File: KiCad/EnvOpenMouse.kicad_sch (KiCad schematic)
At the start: 69 parts, among them J10 FH12 12S 0.5SH, J2 Button, J3 Conn_01x05, J4 Conn_01x09, J5 Conn_02x02_Top_Bottom, J5 SKRKAEE020, J6 Conn_02x02_Top_Bottom, J7 Conn_02x02_Top_Bottom, J8 Conn_02x02_Top_Bottom, J9 Conn_01x03, SW1 SW_Push_SPDT, SW2 SW_Push_SPDT, SW3 SW_Push_SPDT, U1 AP2112K-3.3, U2 TLV70218DBVR, U3 BQ24074RGT, U3 RP2040, U4 PMW3360DM-T2QU, Y1 3225_4P 12MHz

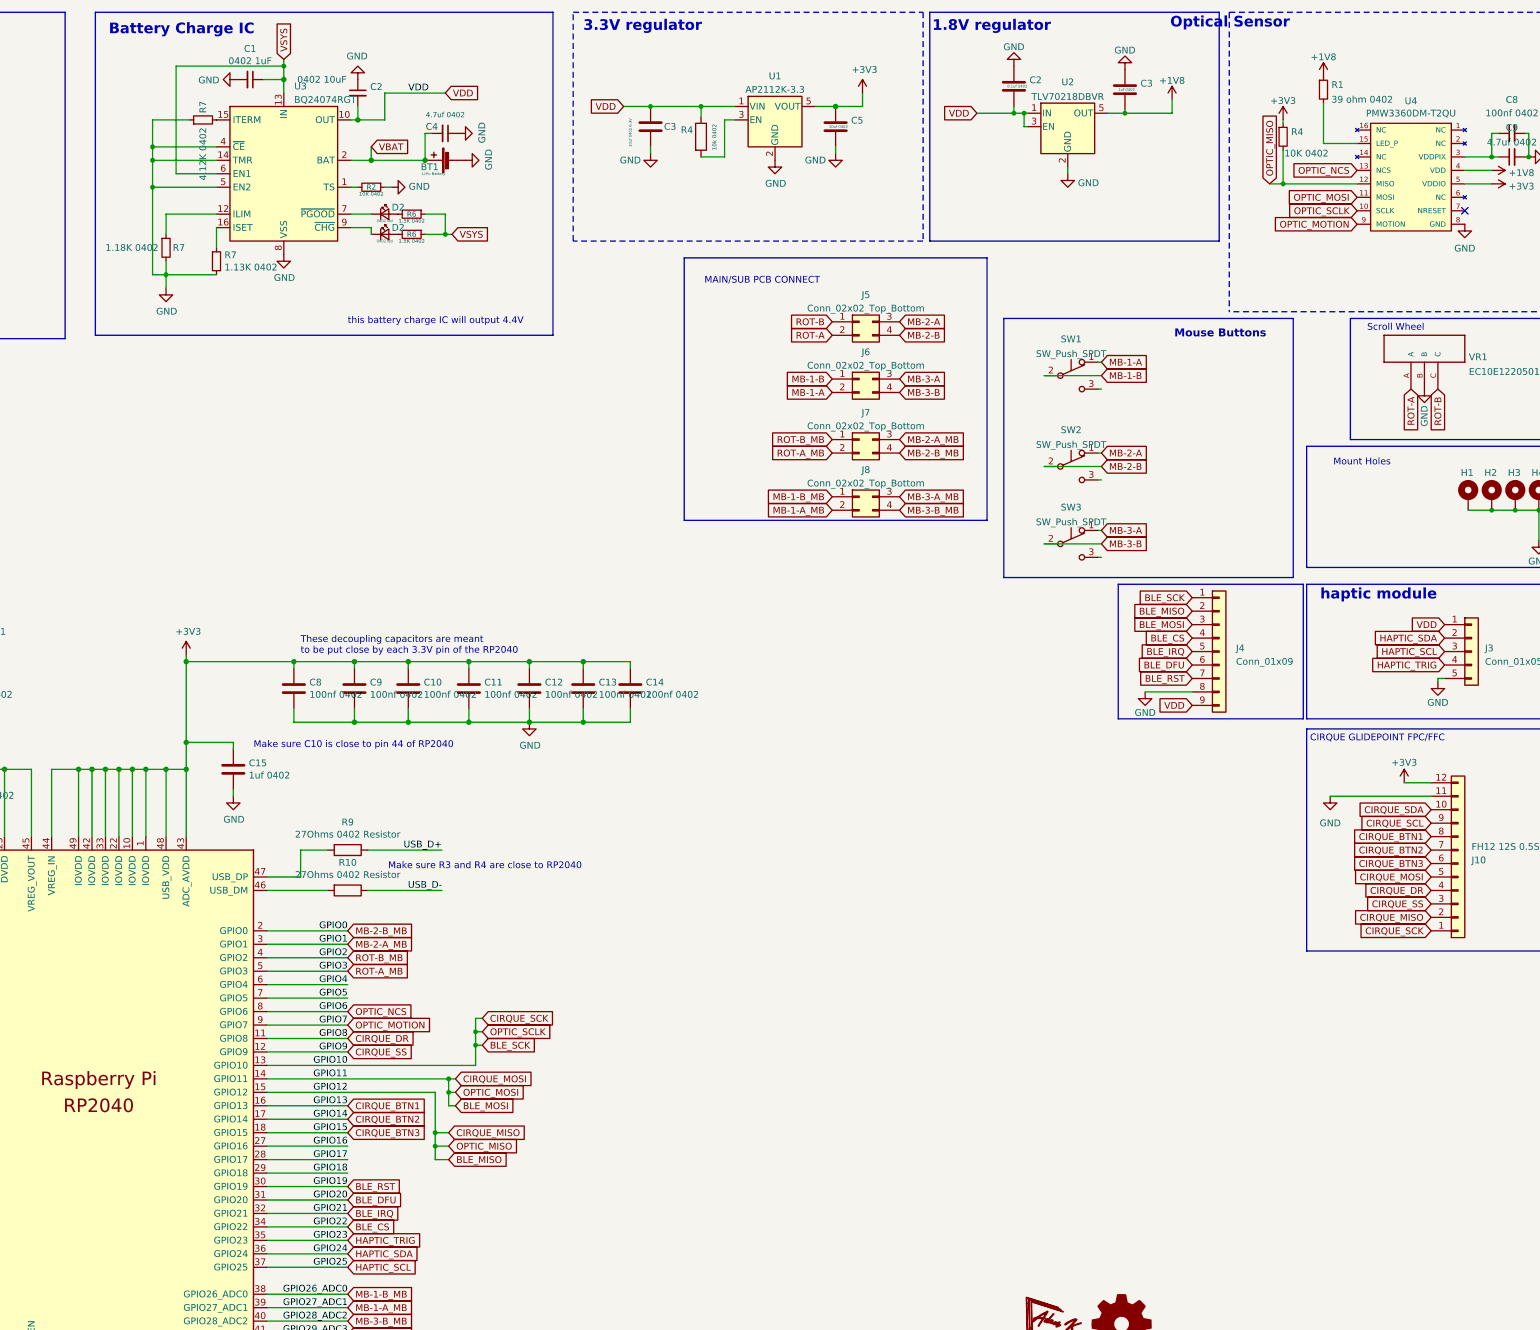
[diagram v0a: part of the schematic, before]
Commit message: re-worked PCB to remove wireless support and battery charge IC
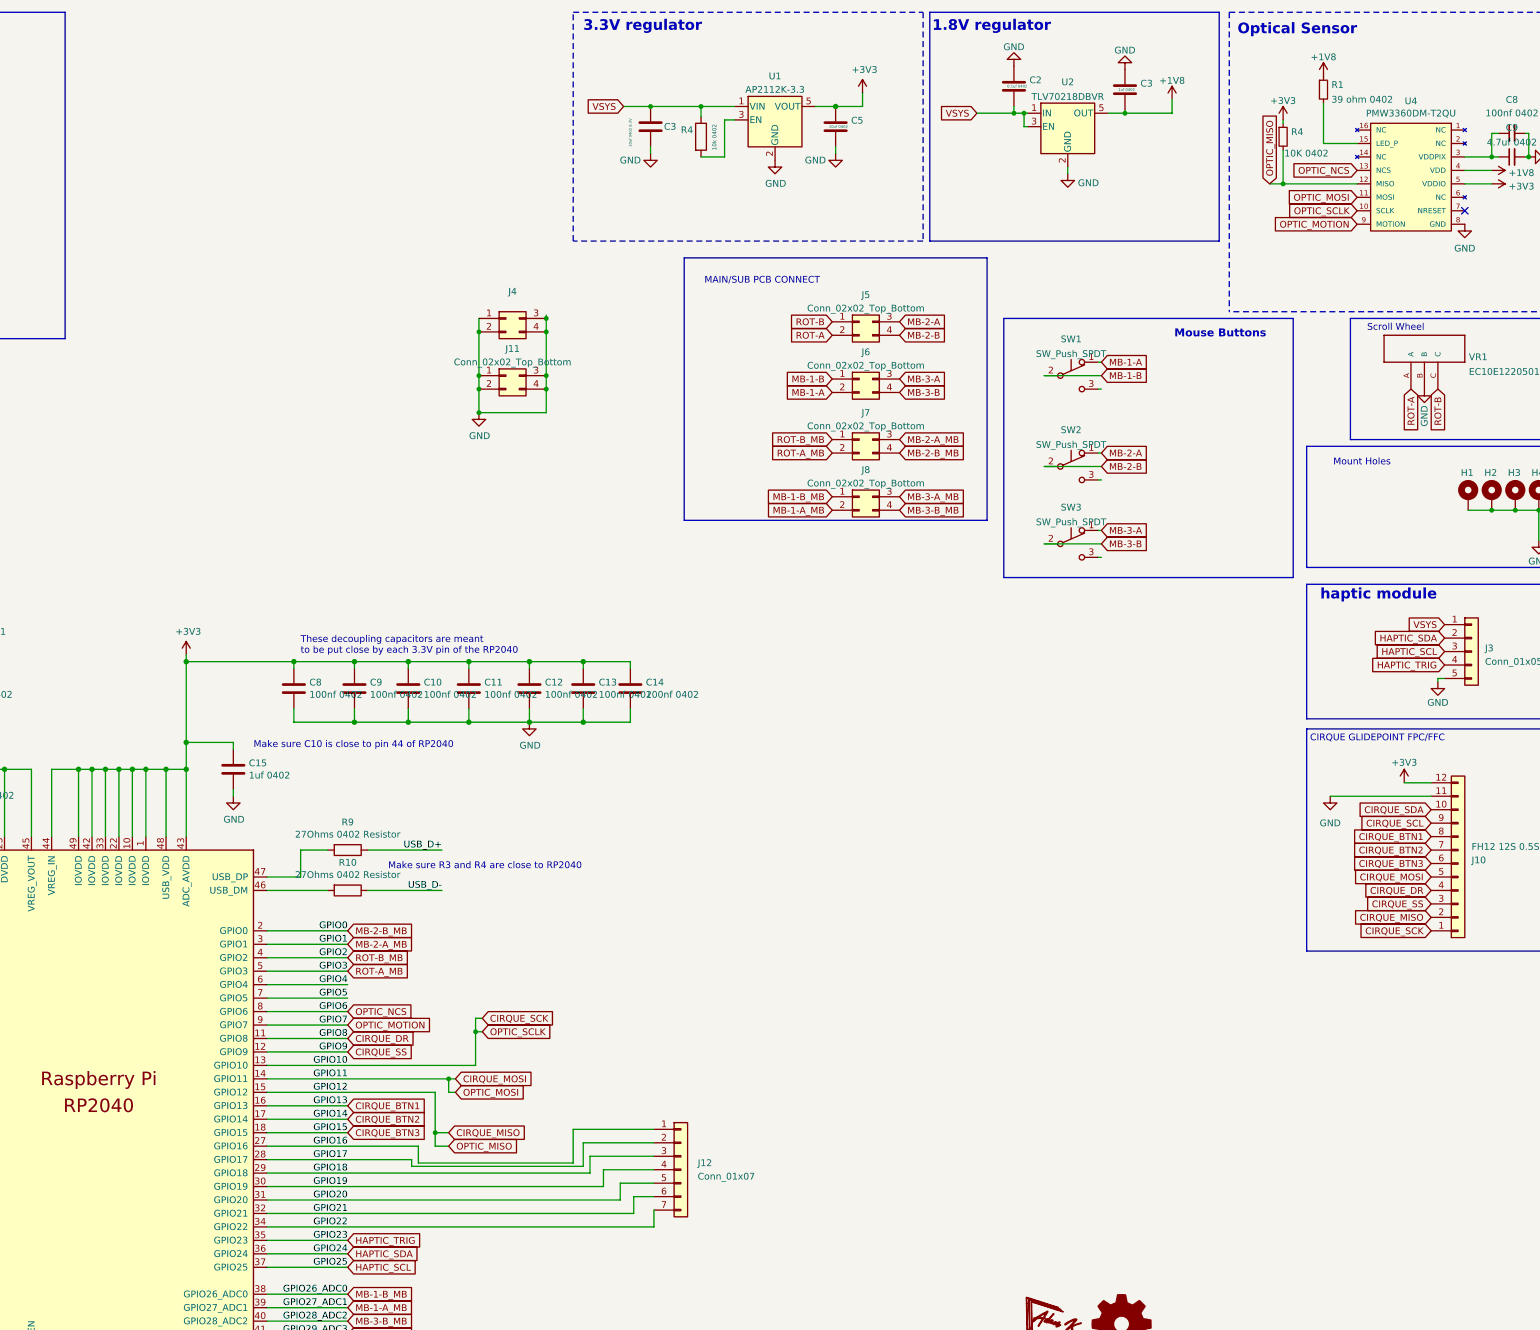
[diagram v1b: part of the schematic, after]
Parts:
- removed BT1: Li-Po Battery, Connector_JST:JST_PH_B2B-PH-K_1x02_P2.00mm_Vertical, symbol Device:Battery_Cell
- removed C1: 0402 1uF, Capacitor_SMD:C_0402_1005Metric, symbol Device:C_Small
- removed C2: 0402 10uF, Resistor_SMD:R_0402_1005Metric, symbol Device:C_Small
- removed C4: 4.7uf 0402, Capacitor_SMD:C_0402_1005Metric, symbol Device:C_Small
- removed D2 (x2): 0402 led, LED_SMD:LED_0402_1005Metric, symbol Device:LED_Small
- removed J4: Conn_01x09, Connector_PinHeader_2.54mm:PinHeader_1x09_P2.54mm_Vertical, symbol Connector_Generic:Conn_01x09
- removed R2: 10K 0402, Resistor_SMD:R_0402_1005Metric, symbol Device:R_Small
- removed R6 (x2): 1.5K 0402, Resistor_SMD:R_0402_1005Metric, symbol Device:R_Small
- removed R7: 1.13K 0402, Resistor_SMD:R_0402_1005Metric, symbol Device:R_Small
- removed R7: 1.18K 0402, Resistor_SMD:R_0402_1005Metric, symbol Device:R_Small
- removed R7: 4.12K 0402, Resistor_SMD:R_0402_1005Metric, symbol Device:R_Small
- removed U3: BQ24074RGT, Package_DFN_QFN:VQFN-16-1EP_3x3mm_P0.5mm_EP1.6x1.6mm, symbol Battery_Management:BQ24074RGT
- added J11, J4: Conn_02x02_Top_Bottom, Connector_PinHeader_1.27mm:PinHeader_1x02_P1.27mm_Vertical, symbol Connector_Generic:Conn_02x02_Top_Bottom
- added J12: Conn_01x07, Connector_PinHeader_1.00mm:PinHeader_1x07_P1.00mm_Vertical, symbol Connector_Generic:Conn_01x07
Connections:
- net VDD is gone; now on net VSYS: C2.2, C3.1, J3.1 (Pin_1), R4.1, U1.1 (VIN), U2.1 (IN), U2.3 (EN)
- net GND: now also J11.1 (Pin_1), J11.2 (Pin_2), J11.3 (Pin_3), J11.4 (Pin_4), J4.1 (Pin_1), J4.2 (Pin_2), J4.3 (Pin_3), J4.4 (Pin_4)
- net GPIO16: now also J12.1 (Pin_1)
- net GPIO17: now also J12.2 (Pin_2)
- net GPIO18: now also J12.3 (Pin_3)
- net BLE_CS renamed GPIO22
- net GPIO22: now also J12.7 (Pin_7)
- net BLE_DFU renamed GPIO20
- net GPIO20: now also J12.5 (Pin_5)
- net BLE_IRQ renamed GPIO21
- net GPIO21: now also J12.6 (Pin_6)
- net BLE_MISO renamed CIRQUE_MISO
- net BLE_MOSI renamed CIRQUE_MOSI
- net BLE_RST renamed GPIO19
- net GPIO19: now also J12.4 (Pin_4)
- net BLE_SCK renamed CIRQUE_SCK
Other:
- note removed: "Battery Charge IC"
- note removed: "this battery charge IC will output 4.4V"

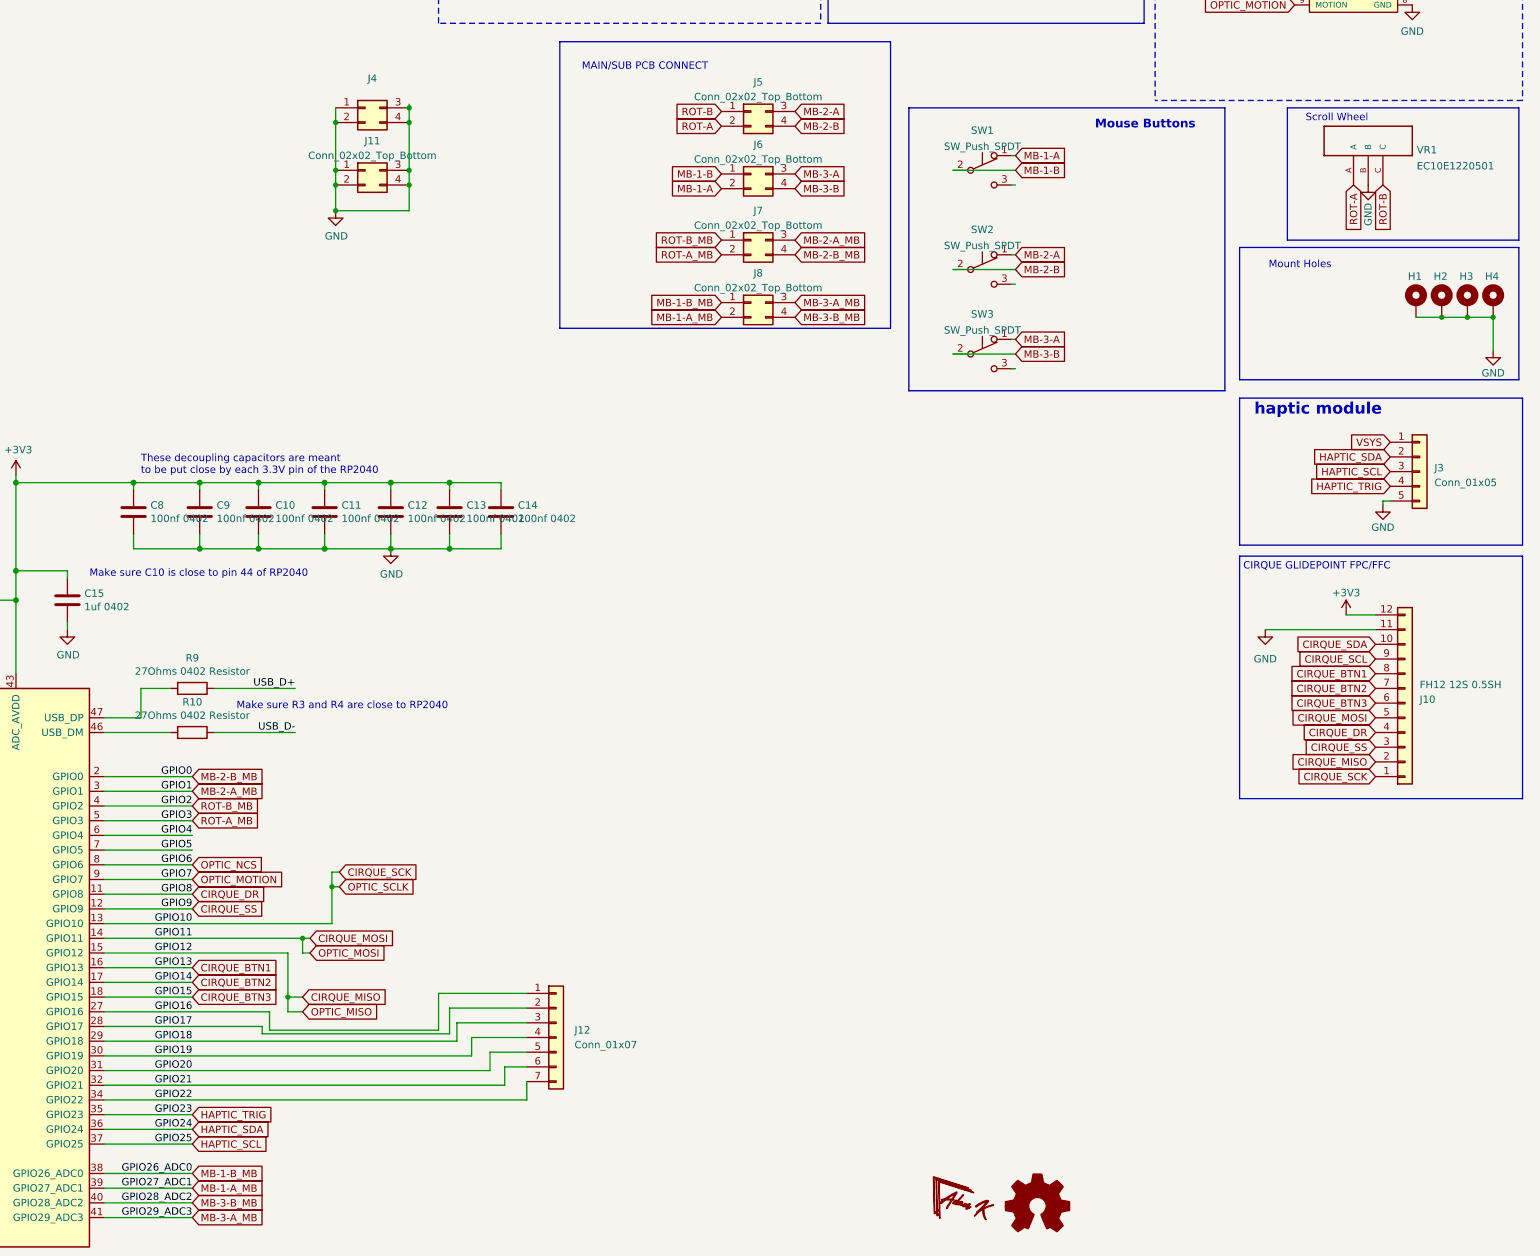
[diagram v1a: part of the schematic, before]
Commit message: removed a bunch of headers, added proper zones for 3v3 and 1v1, would like to add 4x side buttons
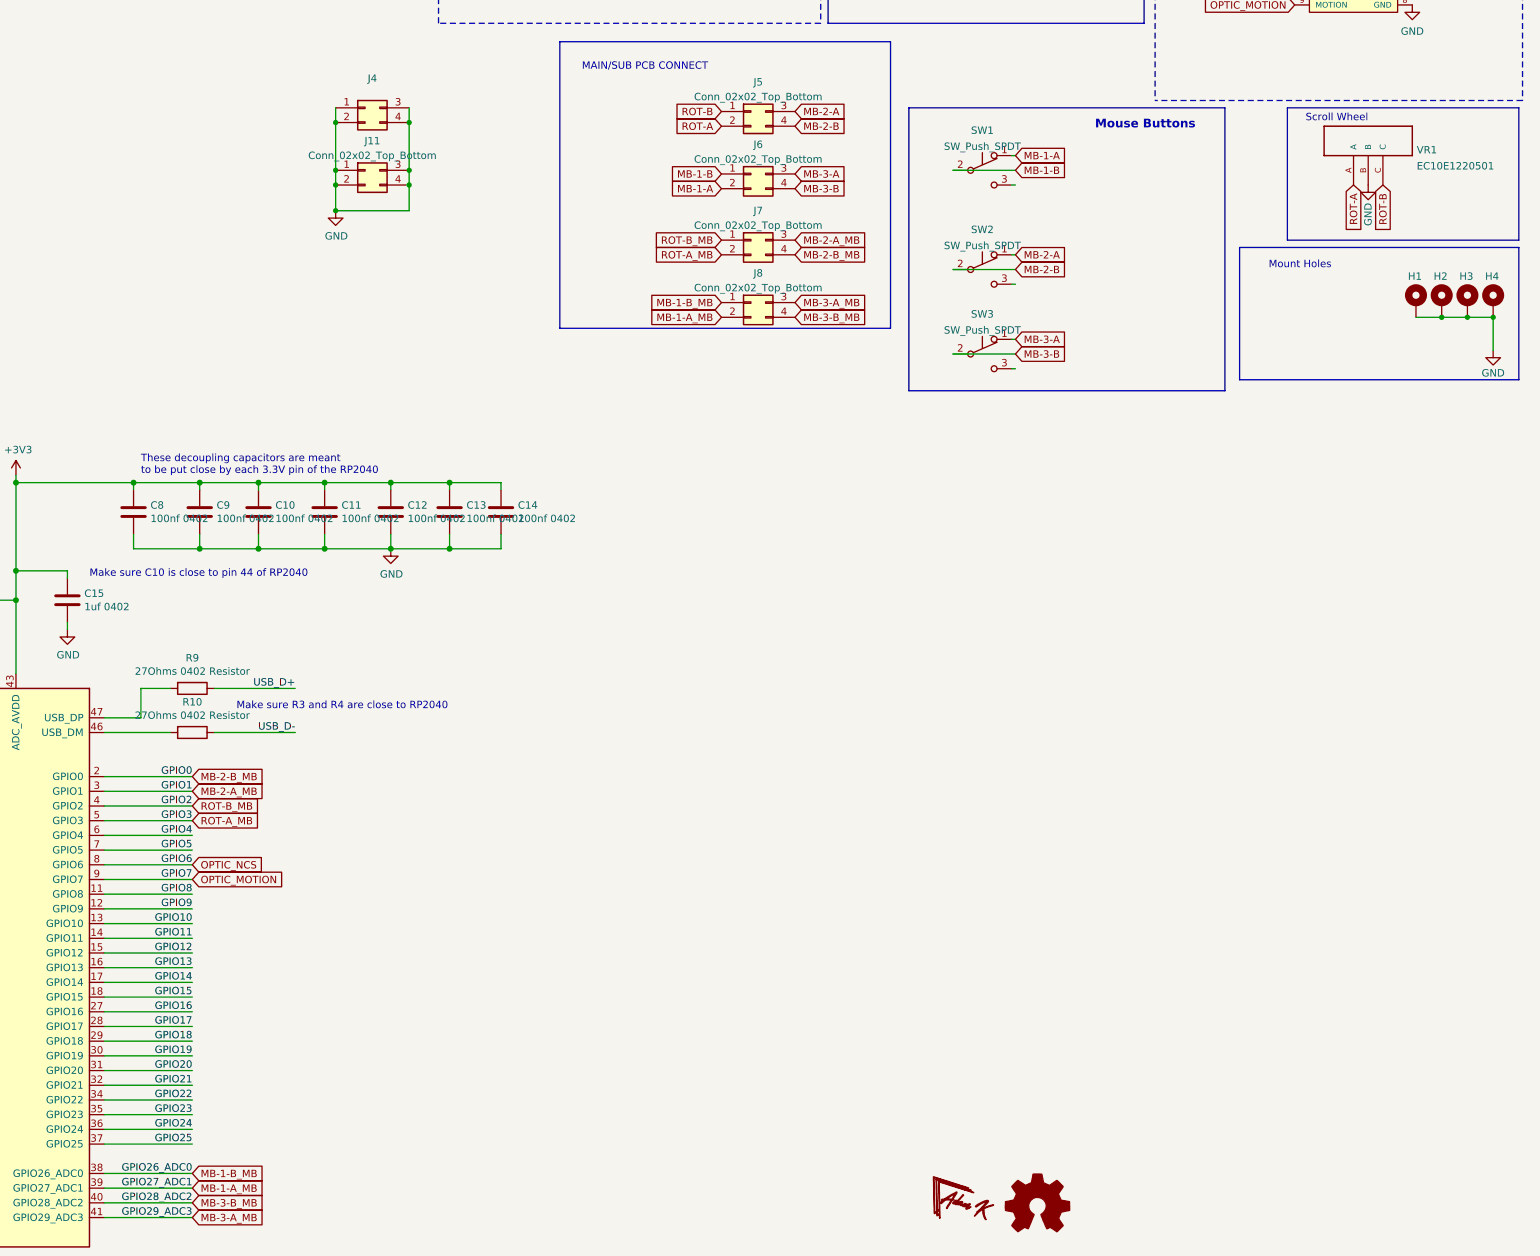
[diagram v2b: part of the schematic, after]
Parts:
- removed J10: FH12 12S 0.5SH, Connector_FFC-FPC:Hirose_FH12-12S-0.5SH_1x12-1MP_P0.50mm_Horizontal, symbol Connector_Generic:Conn_01x12
- removed J12: Conn_01x07, Connector_PinHeader_1.00mm:PinHeader_1x07_P1.00mm_Vertical, symbol Connector_Generic:Conn_01x07
- removed J3: Conn_01x05, Connector_PinHeader_2.54mm:PinHeader_1x05_P2.54mm_Vertical, symbol Connector_Generic:Conn_01x05
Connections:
- net CIRQUE_BTN1 renamed GPIO13
- net CIRQUE_BTN2 renamed GPIO14
- net CIRQUE_BTN3 renamed GPIO15
- net CIRQUE_DR renamed GPIO8
- net CIRQUE_MISO renamed OPTIC_MISO
- net OPTIC_MISO: no longer U3.15 (GPIO12)
- net CIRQUE_MOSI renamed GPIO11
- net GPIO11: no longer U4.11 (MOSI)
- net CIRQUE_SCK renamed GPIO10
- net GPIO10: no longer U4.10 (SCLK)
- net CIRQUE_SS renamed GPIO9
- net HAPTIC_SCL renamed GPIO25
- net HAPTIC_SDA renamed GPIO24
- net HAPTIC_TRIG renamed GPIO23
- new net GPIO12: U3.15 (GPIO12)
- new net OPTIC_MOSI: U4.11 (MOSI)
- new net OPTIC_SCLK: U4.10 (SCLK)
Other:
- note removed: "CIRQUE GLIDEPOINT FPC/FFC"
- note removed: "haptic module"
